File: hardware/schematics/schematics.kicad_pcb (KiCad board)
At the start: 2 copper layers, 99.1 x 97.7 mm, 34 parts, among them J1 Jack-DC, J2 Conn_01x20, J3 Conn_01x20, Q1 IRLD110PBF, U1 ESP32-DevKitC, U2 L7805, U3 MAX6921AUI+

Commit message: Wiring fixed
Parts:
- Q1: footprint Package_DIP:DIP-4_W7.62mm -> Package_DIP:Vishay_HVM-DIP-3_W7.62mm
- moved J3 23.0 mm to (172.7, 57.1), turned to 0 degrees
- moved J2 21.1 mm to (169.5, 92.1), turned to 90 degrees
- moved C3 10.6 mm to (193.7, 139.1)
- moved Q1 7.73 mm to (189.9, 131.4), turned to 0 degrees
- moved REF** 6.99 mm to (204.5, 135.9)
- moved REF** 5.08 mm to (167.6, 134.0)
- moved U2 4.44 mm to (212.1, 143.5)
- moved C5 2.62 mm to (193.7, 147.3)
- moved C7 1.91 mm to (177.2, 120.7)
- moved R3 1.91 mm to (174.6, 123.8)
- moved U3 1.91 mm to (181.0, 113.7)
- moved C2 0.64 mm to (223.5, 146.7)
- moved C1 0.63 mm to (222.2, 143.5)
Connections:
- J2 pad 1: GND -> Net-(J2-Pad1)
- J2 pad 10: /O_4 -> /O_19
- J2 pad 11: /O_19 -> /O_4
- J2 pad 12: /O_3 -> /O_10
- J2 pad 13: /O_18 -> /O_5
- J2 pad 14: /O_2 -> /O_11
- J2 pad 15: /O_17 -> /O_6
- J2 pad 16: /O_1 -> /O_12
- J2 pad 17: /O_16 -> /O_7
- J2 pad 18: /O_0 -> /O_13
- J2 pad 19: Net-(J2-Pad19) -> GND
- J2 pad 2: /O_8 -> GND
- J2 pad 20: GND -> /O_8
- J2 pad 3: /O_13 -> /O_0
- J2 pad 4: /O_7 -> /O_16
- J2 pad 5: /O_12 -> /O_1
- J2 pad 6: /O_6 -> /O_17
- J2 pad 7: /O_11 -> /O_2
- J2 pad 8: /O_5 -> /O_18
- J2 pad 9: /O_10 -> /O_3
- J3 pad 1: /dig_2 -> /fil_v
- J3 pad 10: /seg_h -> /dig_5
- J3 pad 11: /dig_5 -> /seg_h
- J3 pad 12: /seg_a -> /dig_8
- J3 pad 13: /dig_3 -> /seg_d
- J3 pad 14: /seg_f -> /dig_7
- J3 pad 15: /dig_1 -> /seg_c
- J3 pad 16: /seg_b -> /dig_6
- J3 pad 17: /dig_9 -> /seg_e
- J3 pad 18: /seg_g -> /dig_4
- J3 pad 19: Net-(J3-Pad19) -> /fil_g
- J3 pad 20: /fil_v -> /dig_2
- J3 pad 3: /dig_4 -> /seg_g
- J3 pad 4: /seg_e -> /dig_9
- J3 pad 5: /dig_6 -> /seg_b
- J3 pad 6: /seg_c -> /dig_1
- J3 pad 7: /dig_7 -> /seg_f
- J3 pad 8: /seg_d -> /dig_3
- J3 pad 9: /dig_8 -> /seg_a
- R3 pad 1: Net-(J2-Pad19) -> Net-(J2-Pad1)
- U1 pad J3_2: Net-(U1-PadJ3_2) -> /DIN
- U1 pad J3_8: /DIN -> Net-(U1-PadJ3_8)
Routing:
- net Net-(J2-Pad1): track 0.00 -> 38.2 mm
- net Net-(J2-Pad19): track 32.4 -> 0.00 mm
- net /DIN: track 62.4 -> 49.4 mm
- net /LOAD: track 61.9 -> 51.9 mm
- net Net-(D3-Pad2): track 13.2 -> 22.2 mm
- net /PWM: track 35.1 -> 26.7 mm
- net /BLANK: track 53.0 -> 47.0 mm, vias 0 -> 2
- net GND: track 4.47 -> 10.0 mm
- net /CLK: track 55.7 -> 50.3 mm
- net VCC: track 105.0 -> 99.8 mm
- net Net-(U1-PadJ3_8): track 0.00 -> 3.29 mm
- net VBB: track 46.9 -> 49.8 mm
- net /O_8: track 23.4 -> 20.8 mm
- net Net-(U1-PadJ3_5): track 0.00 -> 2.54 mm
- net Net-(U1-PadJ3_4): track 0.00 -> 2.54 mm
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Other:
- outline, holes or cut-outs redrawn
- board text added: "Hiroto Kaku 2021 Callisto - Main PCB"
- board text removed: "Hiroto Kaku 2021 Callisto - Main Board"

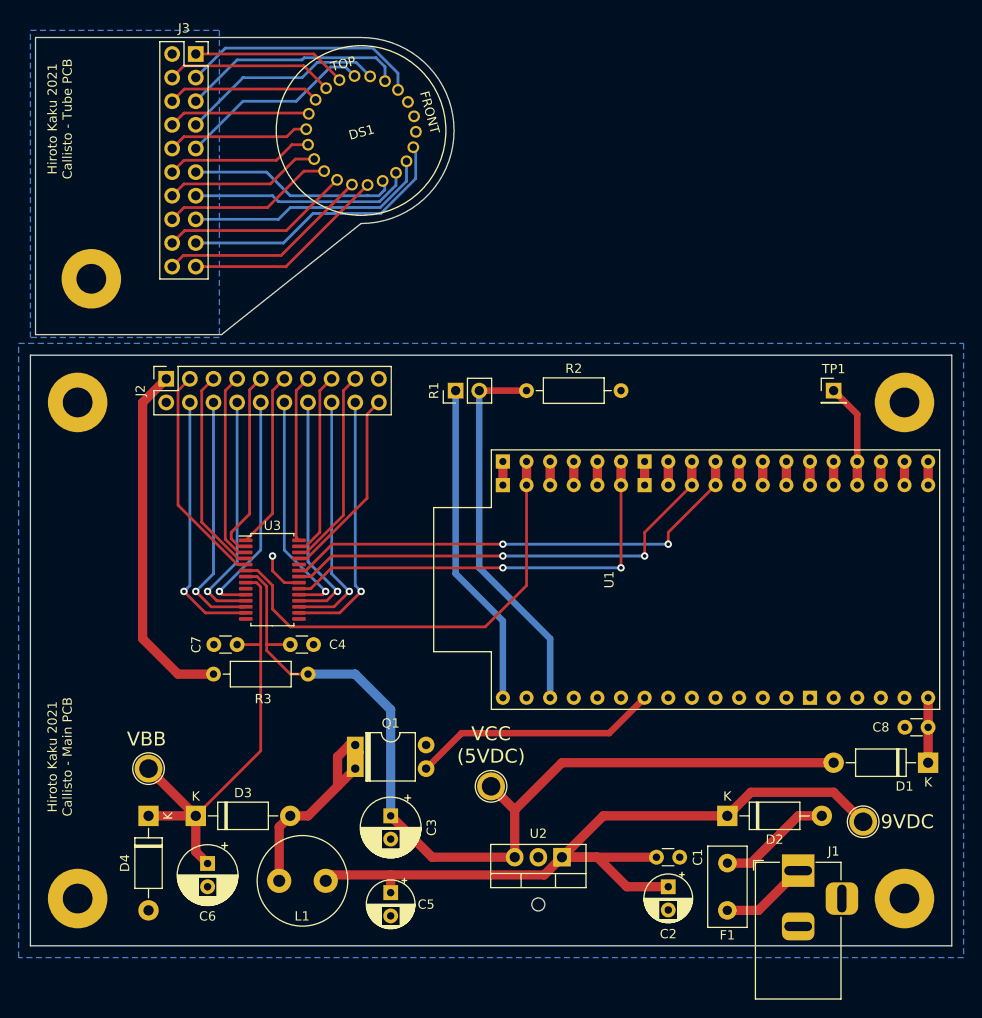
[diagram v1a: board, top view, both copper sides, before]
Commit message: Revision 2 of PCB, hopefully without workarounds
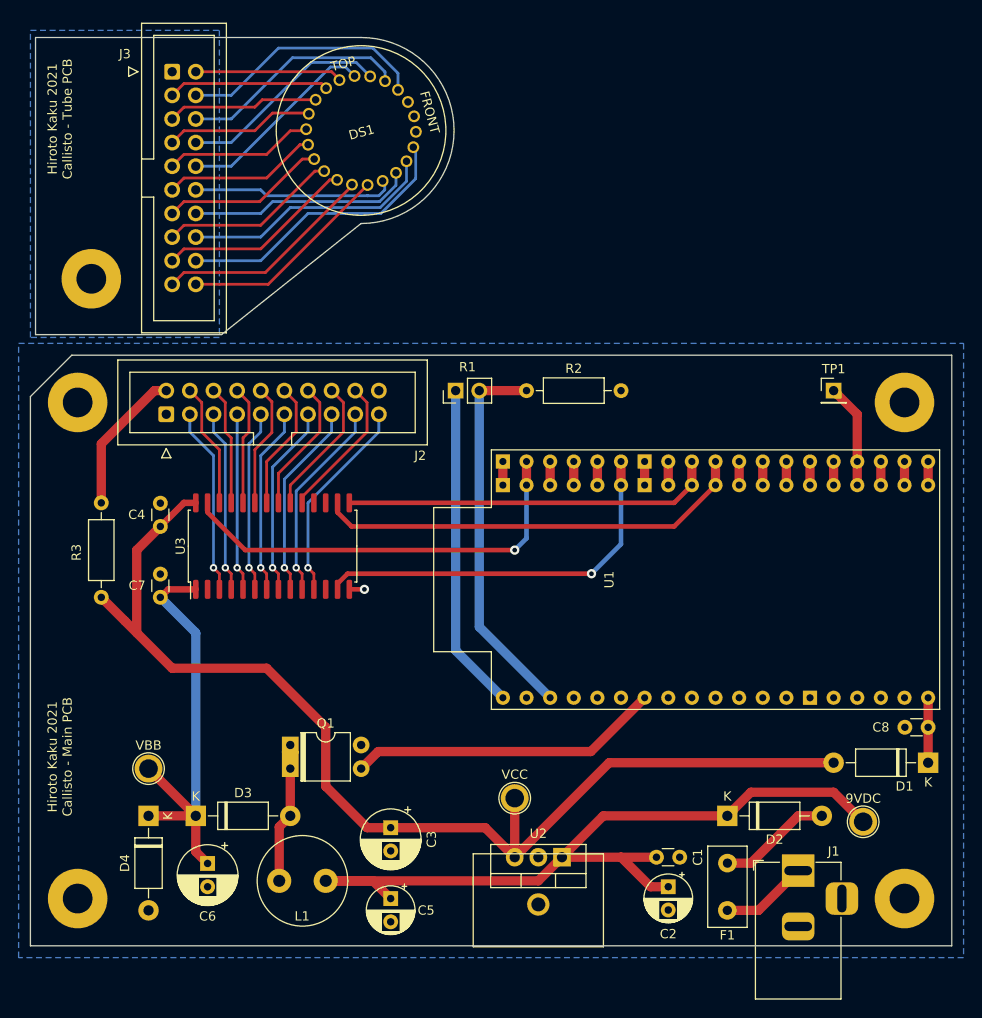
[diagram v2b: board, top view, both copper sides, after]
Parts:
- J2, J3: footprint Connector_PinSocket_2.54mm:PinSocket_2x10_P2.54mm_Vertical -> Connector_IDC:IDC-Header_2x10_P2.54mm_Vertical
- U2: footprint Package_TO_SOT_THT:TO-220-3_Vertical -> callisto:L7805_with_heatsink
- U3: value MAX6921AUI+ -> MAX6921AWI+; footprint Package_SO:TSSOP-28_4.4x9.7mm_P0.65mm -> Package_SO:SOIC-28W_7.5x17.9mm_P1.27mm
- moved R3 22.0 mm to (162.6, 105.4), turned to 270 degrees
- moved C4 18.9 mm to (168.9, 108.0), turned to 90 degrees
- moved C7 9.69 mm to (168.9, 115.6), turned to 90 degrees
- moved Q1 6.99 mm to (182.9, 131.4)
- moved J2 3.81 mm to (169.5, 95.9)
- moved U3 3.61 mm to (181.0, 110.1), turned to 90 degrees
- moved J3 3.17 mm to (170.2, 59.1)
- moved VCC 2.84 mm to (207.0, 137.2)
- moved C3 1.27 mm to (193.7, 140.3)
- moved C5 0.64 mm to (193.7, 148.0)
- renumbered REF** to 9VDC, REF** to VBB, REF** to VCC
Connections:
- J2 pad 1: Net-(J2-Pad1) -> GND
- J2 pad 10: /O_19 -> /O_3
- J2 pad 11: /O_4 -> /O_15
- J2 pad 12: /O_10 -> /O_4
- J2 pad 13: /O_5 -> /O_14
- J2 pad 14: /O_11 -> /O_5
- J2 pad 15: /O_6 -> /O_13
- J2 pad 16: /O_12 -> /O_6
- J2 pad 17: /O_7 -> /O_12
- J2 pad 18: /O_13 -> /O_7
- J2 pad 19: GND -> /O_11
- J2 pad 2: GND -> Net-(J2-Pad2)
- J2 pad 20: /O_8 -> GND
- J2 pad 3: /O_0 -> /O_19
- J2 pad 4: /O_16 -> /O_0
- J2 pad 5: /O_1 -> /O_18
- J2 pad 6: /O_17 -> /O_1
- J2 pad 7: /O_2 -> /O_17
- J2 pad 8: /O_18 -> /O_2
- J2 pad 9: /O_3 -> /O_16
- J3 pad 1: /fil_v -> /fil_g
- J3 pad 10: /dig_5 -> /seg_a
- J3 pad 11: /seg_h -> /dig_8
- J3 pad 12: /dig_8 -> /seg_h
- J3 pad 13: /seg_d -> /dig_7
- J3 pad 14: /dig_7 -> /seg_d
- J3 pad 15: /seg_c -> /dig_6
- J3 pad 16: /dig_6 -> /seg_c
- J3 pad 17: /seg_e -> /dig_4
- J3 pad 18: /dig_4 -> /seg_e
- J3 pad 19: /fil_g -> /dig_2
- J3 pad 2: /fil_g -> /fil_v
- J3 pad 20: /dig_2 -> /fil_g
- J3 pad 3: /seg_g -> /dig_9
- J3 pad 4: /dig_9 -> /seg_g
- J3 pad 5: /seg_b -> /dig_1
- J3 pad 6: /dig_1 -> /seg_b
- J3 pad 7: /seg_f -> /dig_3
- J3 pad 8: /dig_3 -> /seg_f
- J3 pad 9: /seg_a -> /dig_5
- R3 pad 1: Net-(J2-Pad1) -> Net-(J2-Pad2)
- U3 pad 1: /O_4 -> VBB
- U3 pad 10: /O_19 -> /O_12
- U3 pad 11: /O_18 -> /O_11
- U3 pad 12: /O_17 -> Net-(U3-Pad12)
- U3 pad 13: /O_16 -> /BLANK
- U3 pad 14: Net-(U3-Pad14) -> GND
- U3 pad 15: Net-(U3-Pad15) -> /CLK
- U3 pad 16: /O_13 -> /LOAD
- U3 pad 17: /O_12 -> Net-(U3-Pad17)
- U3 pad 18: /O_11 -> Net-(U3-Pad18)
- U3 pad 19: /O_10 -> /O_7
- U3 pad 2: /O_3 -> /DOUT
- U3 pad 20: /BLANK -> /O_6
- U3 pad 21: GND -> /O_5
- U3 pad 22: /CLK -> /O_4
- U3 pad 23: /LOAD -> /O_3
- U3 pad 24: Net-(U3-Pad24) -> /O_2
- U3 pad 25: /O_8 -> /O_1
- U3 pad 26: /O_7 -> /O_0
- U3 pad 27: /O_6 -> /DIN
- U3 pad 28: /O_5 -> VCC
- U3 pad 3: /O_2 -> /O_19
- U3 pad 4: /O_1 -> /O_18
- U3 pad 5: /O_0 -> /O_17
- U3 pad 6: /DIN -> /O_16
- U3 pad 7: VCC -> /O_15
- U3 pad 8: VBB -> /O_14
- U3 pad 9: Net-(U3-Pad9) -> /O_13
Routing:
- net Net-(J2-Pad1): track 38.2 -> 0.00 mm
- net /O_10: track 25.2 -> 0.00 mm, vias 1 -> 0
- net VCC: track 99.8 -> 121.9 mm
- net /O_8: track 20.8 -> 0.00 mm
- net /O_14: track 0.00 -> 20.7 mm, vias 0 -> 1
- net /O_15: track 0.00 -> 20.1 mm, vias 0 -> 1
- net Net-(J2-Pad2): track 0.00 -> 15.7 mm
- net /O_0: track 24.0 -> 13.4 mm
- net /CLK: track 50.3 -> 40.2 mm, vias 2 -> 0
- net /O_1: track 22.3 -> 12.9 mm
- net /O_16: track 28.2 -> 19.6 mm
- net /O_17: track 27.2 -> 19.1 mm
- net /O_2: track 20.6 -> 12.9 mm
- net /O_3: track 20.4 -> 13.3 mm
- net Net-(D3-Pad2): track 22.2 -> 15.1 mm
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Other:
- outline, holes or cut-outs redrawn
- board text removed: "9VDC"
- board text removed: "VBB"
- board text removed: "VCC (5VDC)"

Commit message: updated to KiCad 6
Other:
- net class Default removed
